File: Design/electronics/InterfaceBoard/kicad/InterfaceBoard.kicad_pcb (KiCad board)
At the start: 2 copper layers, 22 parts, among them J1 Screw_Terminal_1x02, J10 Screw_Terminal_1x02, J11 CONN_01X03, J12 Screw_Terminal_1x02, J13 CONN_01X03, J2 Screw_Terminal_1x02, J3 Screw_Terminal_1x02, J4 Screw_Terminal_1x02, J5 Screw_Terminal_1x02, J6 Screw_Terminal_1x02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

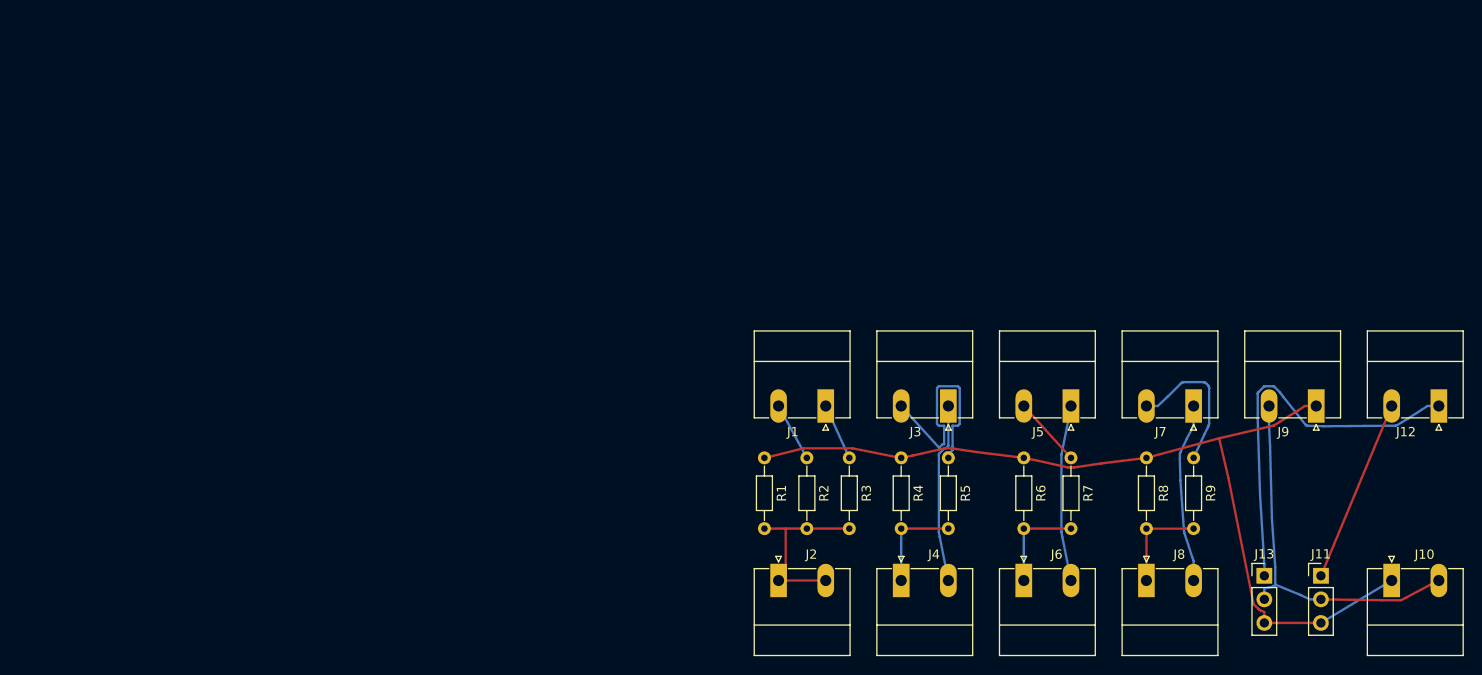
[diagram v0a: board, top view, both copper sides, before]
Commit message: Updated the veroboard circuits Updated the interface board design updated the RS parts list
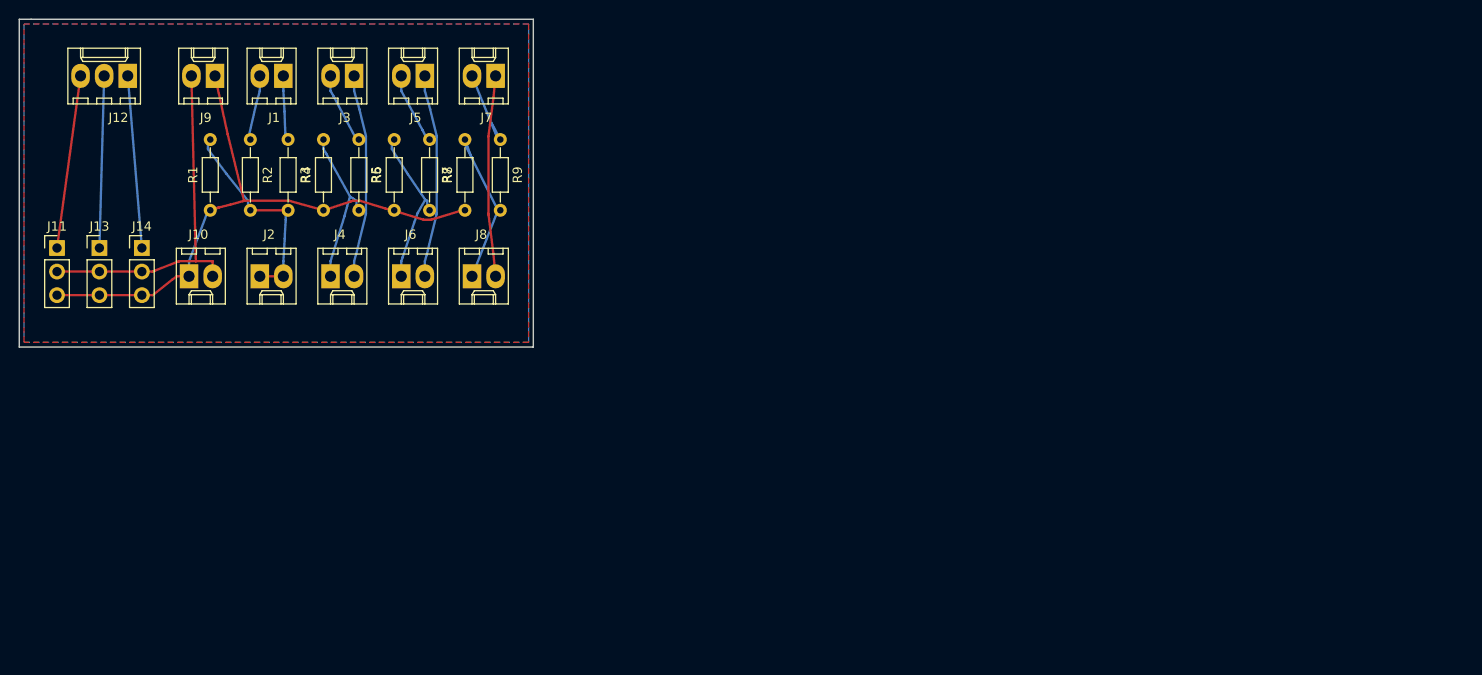
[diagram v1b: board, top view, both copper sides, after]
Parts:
- added J14: FIRE, Pin_Headers:Pin_Header_Straight_1x03_Pitch2.54mm, F.Cu at (61.5, 85.1)
- J1, J2: value Screw_Terminal_1x02 -> PROX1; footprint Connectors_Phoenix:PhoenixContact_MC-G_02x5.08mm_Angled -> Connectors_Molex:Molex_KK-6410-02_02x2.54mm_Straight
- J10: value Screw_Terminal_1x02 -> PWR OUT; footprint Connectors_Phoenix:PhoenixContact_MC-G_02x5.08mm_Angled -> Connectors_Molex:Molex_KK-6410-02_02x2.54mm_Straight
- J11: value CONN_01X03 -> HORZ
- J12: value Screw_Terminal_1x02 -> SERVO_IN; footprint Connectors_Phoenix:PhoenixContact_MC-G_02x5.08mm_Angled -> Connectors_Molex:Molex_KK-6410-03_03x2.54mm_Straight
- J13: value CONN_01X03 -> VERT
- J3, J4: value Screw_Terminal_1x02 -> PROX2; footprint Connectors_Phoenix:PhoenixContact_MC-G_02x5.08mm_Angled -> Connectors_Molex:Molex_KK-6410-02_02x2.54mm_Straight
- J5, J6: value Screw_Terminal_1x02 -> PROX3; footprint Connectors_Phoenix:PhoenixContact_MC-G_02x5.08mm_Angled -> Connectors_Molex:Molex_KK-6410-02_02x2.54mm_Straight
- J7, J8: value Screw_Terminal_1x02 -> PROX4; footprint Connectors_Phoenix:PhoenixContact_MC-G_02x5.08mm_Angled -> Connectors_Molex:Molex_KK-6410-02_02x2.54mm_Straight
- J9: value Screw_Terminal_1x02 -> PWR IN; footprint Connectors_Phoenix:PhoenixContact_MC-G_02x5.08mm_Angled -> Connectors_Molex:Molex_KK-6410-02_02x2.54mm_Straight
- moved J12 145.6 mm to (59.9, 66.5)
- moved J11 140.6 mm to (52.3, 85.1)
- moved J10 133.6 mm to (66.5, 88.1)
- moved J13 130.3 mm to (56.9, 85.1)
- moved J9 123.8 mm to (69.3, 66.5)
- moved J7 83.2 mm to (99.6, 66.5)
- moved R9 82.2 mm to (100.1, 73.4)
- moved J8 79.7 mm to (97.0, 88.1)
- moved J5 78.2 mm to (91.9, 66.5)
- moved R8 78.1 mm to (96.3, 81.0), turned to 90 degrees
- moved R7 77.1 mm to (92.5, 73.4)
- moved J6 74.6 mm to (89.4, 88.1)
- moved J3 73.2 mm to (84.3, 66.5)
- moved R6 72.9 mm to (88.6, 81.0), turned to 90 degrees
- moved R5 72.2 mm to (84.8, 73.4)
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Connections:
- J12 pad 2: Net-(J11-Pad1) -> Net-(J12-Pad2)
- J13 pad 1: Net-(J12-Pad1) -> Net-(J12-Pad2)
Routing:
- net GND: track 96.9 -> 66.1 mm
- net Net-(J12-Pad1): track 42.1 -> 18.6 mm
- net Net-(J12-Pad2): track 0.00 -> 18.5 mm
- net Net-(J3-Pad2): track 25.0 -> 7.81 mm
- net Net-(J6-Pad1): track 10.7 -> 18.4 mm
- net Net-(J8-Pad1): track 10.7 -> 18.4 mm
- net Net-(J4-Pad1): track 10.7 -> 18.2 mm
- net Net-(J7-Pad2): track 16.0 -> 9.74 mm
- net Net-(J2-Pad1): track 19.8 -> 24.2 mm
- net Net-(J5-Pad1): track 19.0 -> 21.9 mm
- net Net-(J3-Pad1): track 19.4 -> 21.9 mm
- net Net-(J7-Pad1): track 19.3 -> 21.7 mm
- net +5V: track 40.2 -> 38.6 mm
- net Net-(J1-Pad1): track 6.14 -> 7.57 mm
- net Net-(J11-Pad1): track 19.8 -> 18.7 mm
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- added copper zone on B.Cu, net GND
- added copper zone on F.Cu, net GND
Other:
- board outline added: 55.4 x 35.3 mm
